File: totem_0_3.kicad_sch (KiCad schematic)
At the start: 52 parts, among them J1 MJ-4PP-9, J2 MJ-4PP-9, U1 xiao-ble, U2 xiao-ble, U3 RP2040, U4 RP2040

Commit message: Split MCU aux schemas into own sheet
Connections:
- net GND_L: now also U3.57 (GND)
- net GND_R: now also U4.57 (GND)
- net 3V3_REG_L: now reaches U3.1 (IOVDD), U3.10 (IOVDD), U3.22 (IOVDD), U3.33 (IOVDD), U3.42 (IOVDD), U3.49 (IOVDD)
- net 3V3_REG_L: now also U3.43 (ADC_AVDD), U3.44 (VREG_IN), U3.48 (USB_VDD)
- net XIN_L: now reaches U3.20 (XIN)
- net XOUT_L: now reaches U3.21 (XOUT)
- net USB_L_D-: now reaches U3.46 (USB_DM)
- net USB_L_D-: now also U4.46 (USB_DM)
- net USB_L_D+: now reaches U3.47 (USB_DP)
- net USB_L_D+: now also U4.47 (USB_DP)
- net 3V3_REG_R: now reaches U4.1 (IOVDD), U4.10 (IOVDD), U4.22 (IOVDD), U4.33 (IOVDD), U4.42 (IOVDD), U4.49 (IOVDD)
- net 3V3_REG_R: now also U4.43 (ADC_AVDD), U4.44 (VREG_IN), U4.48 (USB_VDD)
- net XIN_R: now reaches U4.20 (XIN)
- net XOUT_R: now reaches U4.21 (XOUT)
- net VREG_R: now reaches U4.23 (DVDD), U4.50 (DVDD)
- net VREG_R: now also U4.45 (VREG_VOUT)
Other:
- added sheet MCU auxiliaries (mcu_auxiliaries.kicad_sch)
- moved on the sheet: BAT+1, BAT+2, BATGND1, BATGND2, J1, J2, PSW1, PSW2, RSW1, RSW2, SWL1, SWL10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

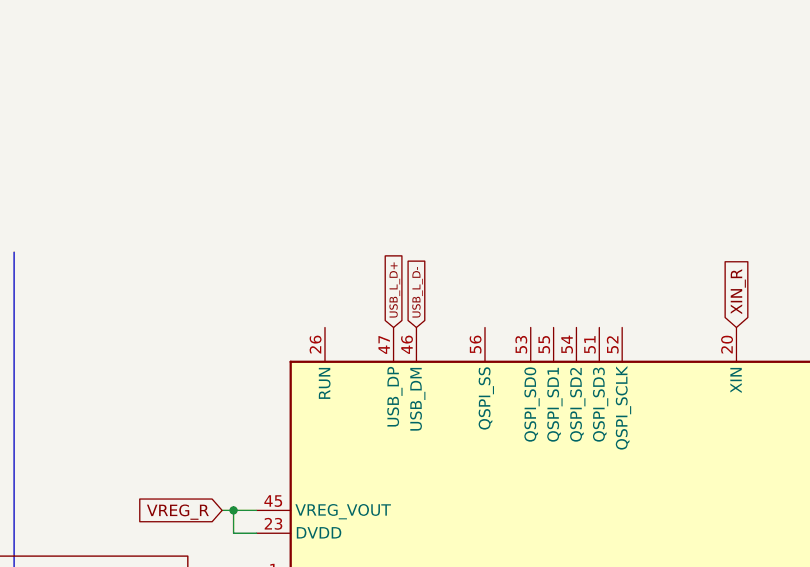
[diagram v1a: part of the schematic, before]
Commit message: fix right usb labels
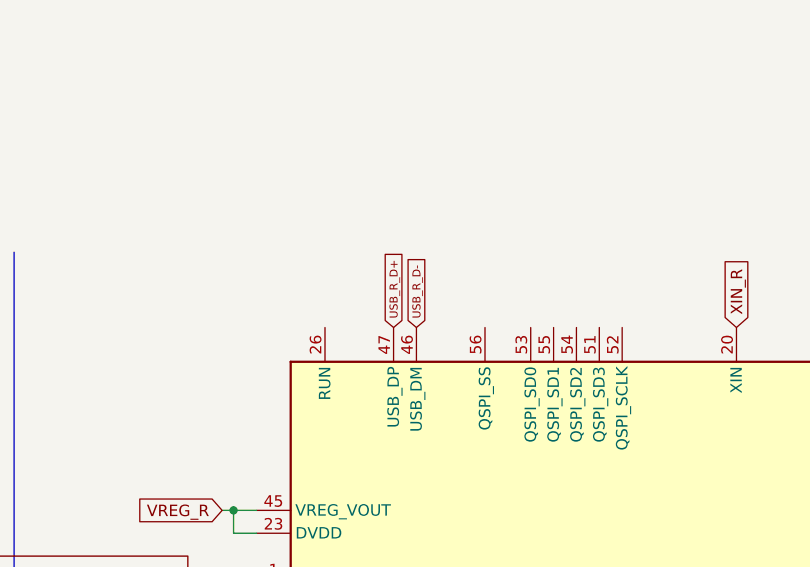
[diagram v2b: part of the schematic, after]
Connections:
- net USB_L_D+: no longer U4.47 (USB_DP)
- net USB_L_D-: no longer U4.46 (USB_DM)
- new net USB_R_D+: U4.47 (USB_DP)
- new net USB_R_D-: U4.46 (USB_DM)
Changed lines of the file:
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@@
 		)
 	)
-	(global_label "USB_L_D-"
+	(global_label "USB_R_D-"
 		(shape input)
 		(at 193.04 20.32 90)
@@
 		)
 		(property "Intersheetrefs" "${INTERSHEET_REFS}"
-			(at 193.04 11.4995 90)
+			(at 193.04 11.3302 90)
 			(effects
 				(font
@@
 		)
 	)
-	(global_label "USB_L_D+"
+	(global_label "USB_R_D+"
 		(shape input)
 		(at 190.5 20.32 90)
@@
 		)
 		(property "Intersheetrefs" "${INTERSHEET_REFS}"
-			(at 190.5 11.4995 90)
+			(at 190.5 11.3302 90)
 			(effects
 				(font

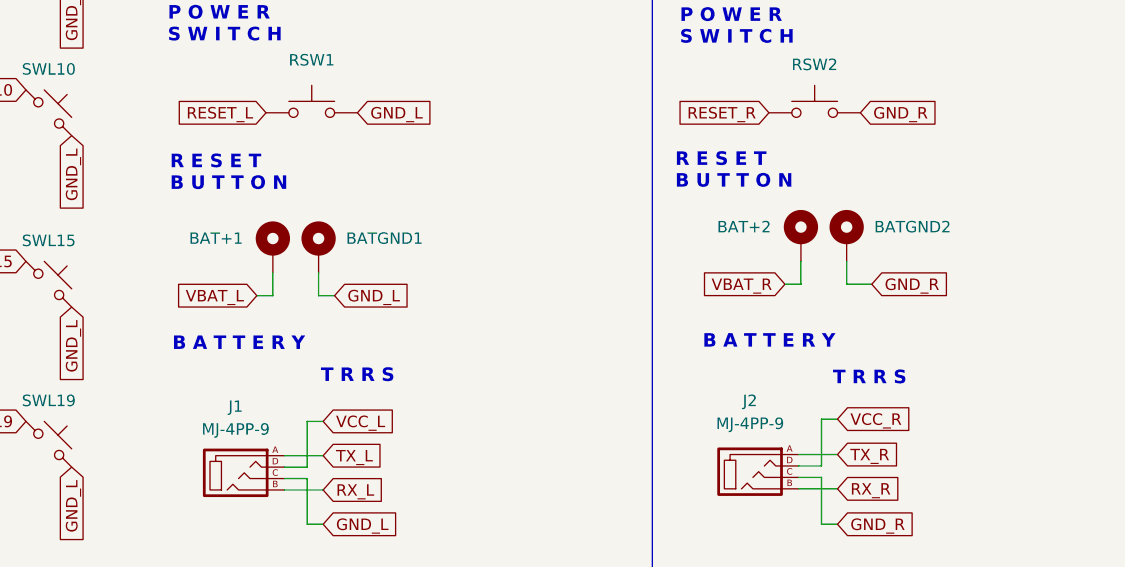
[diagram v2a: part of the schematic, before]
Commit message: Remove battery from schema
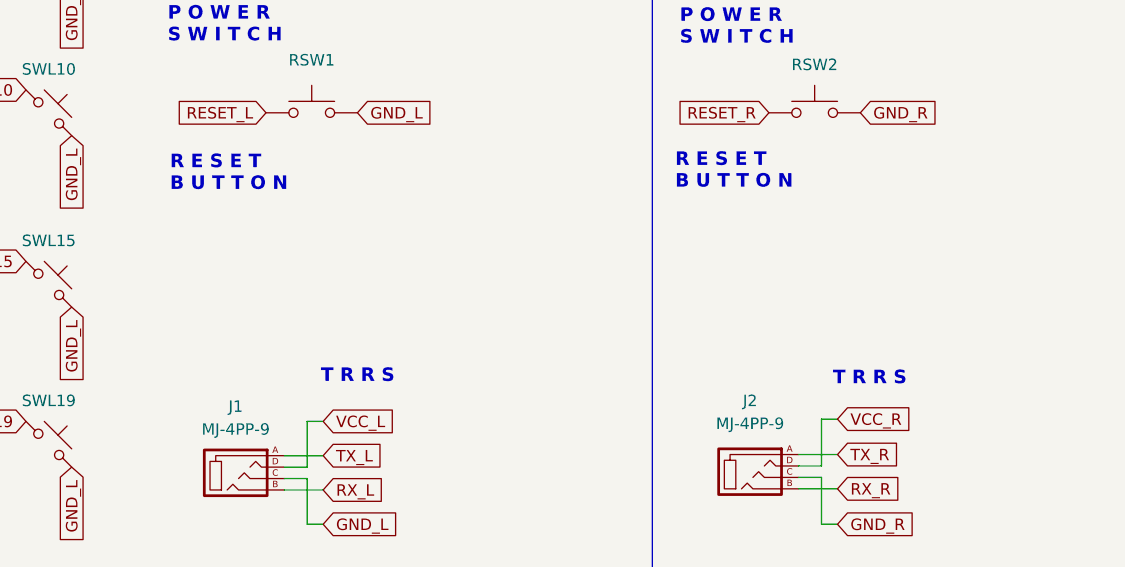
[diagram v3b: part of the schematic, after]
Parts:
- removed BAT+1, BAT+2: +, TOTEMlib:BatteryPad, symbol Mechanical:MountingHole_Pad
- removed BATGND1, BATGND2: -, TOTEMlib:BatteryPad, symbol Mechanical:MountingHole_Pad
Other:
- note removed: "B A T T E R Y"

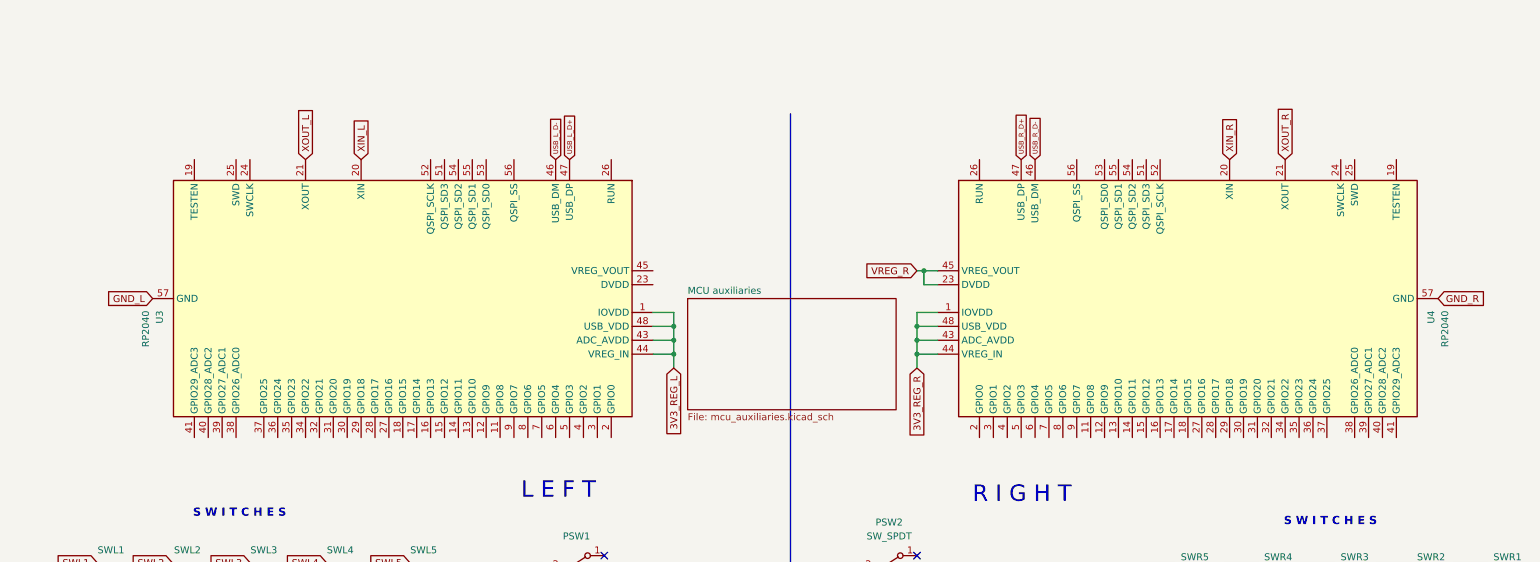
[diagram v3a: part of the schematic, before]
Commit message: Add qspi flash
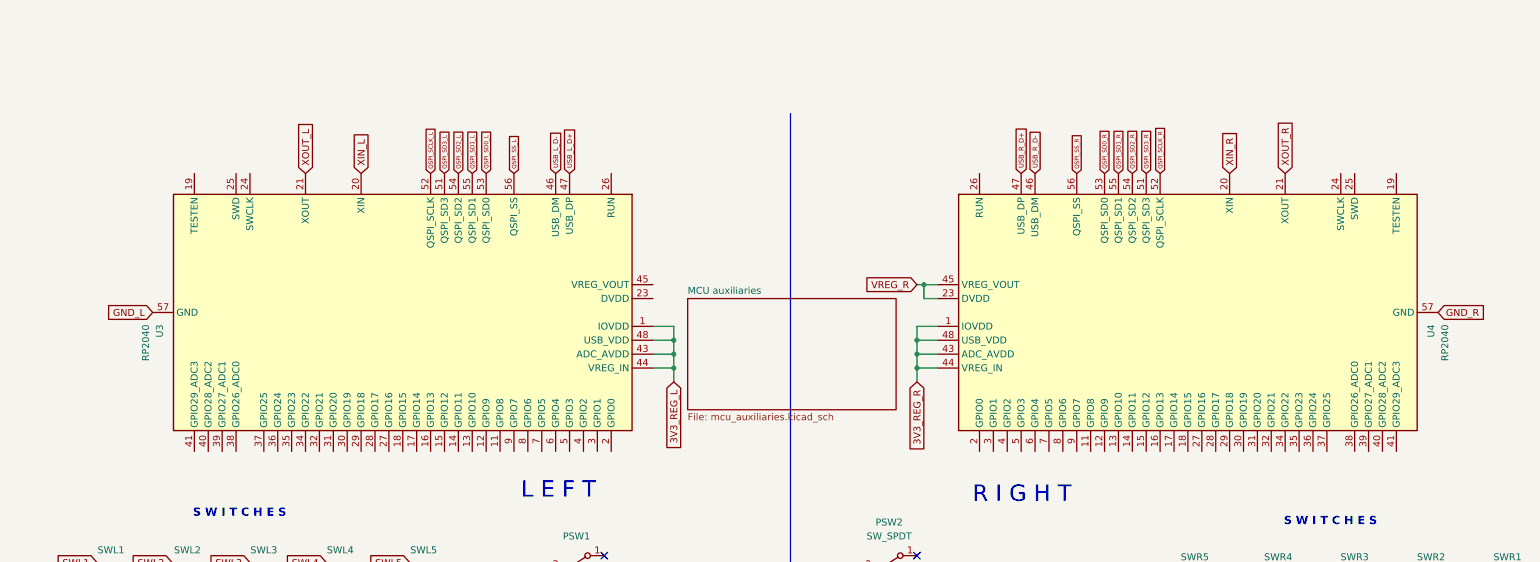
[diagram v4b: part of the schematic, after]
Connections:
- net QSPI_SD3_L: now reaches U3.51 (QSPI_SD3)
- net QSPI_SCLK_L: now reaches U3.52 (QSPI_SCLK)
- net QSPI_SD0_L: now reaches U3.53 (QSPI_SD0)
- net QSPI_SD2_L: now reaches U3.54 (QSPI_SD2)
- net QSPI_SD1_L: now reaches U3.55 (QSPI_SD1)
- net QSPI_SS_L: now reaches U3.56 (QSPI_SS)
- net QSPI_SD3_R: now reaches U4.51 (QSPI_SD3)
- net QSPI_SCLK_R: now reaches U4.52 (QSPI_SCLK)
- net QSPI_SD0_R: now reaches U4.53 (QSPI_SD0)
- net QSPI_SD2_R: now reaches U4.54 (QSPI_SD2)
- net QSPI_SD1_R: now reaches U4.55 (QSPI_SD1)
- net QSPI_SS_R: now reaches U4.56 (QSPI_SS)
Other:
- moved on the sheet: U3, U4

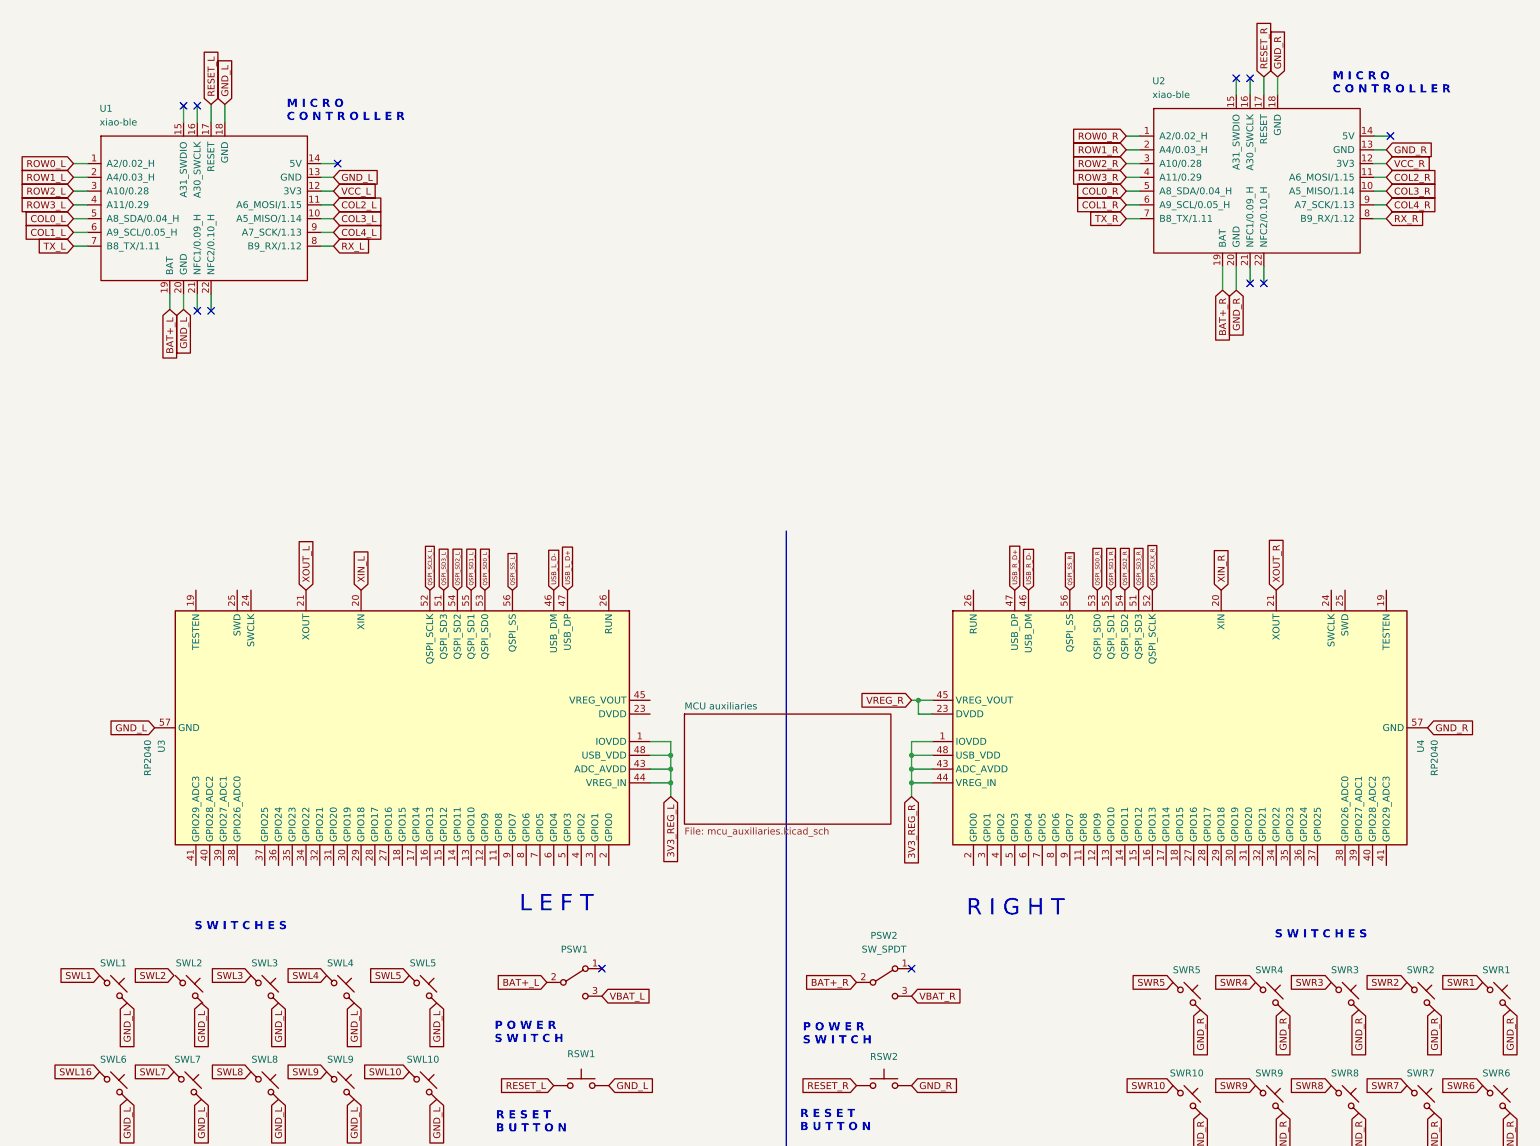
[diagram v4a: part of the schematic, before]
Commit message: Remove old mcu
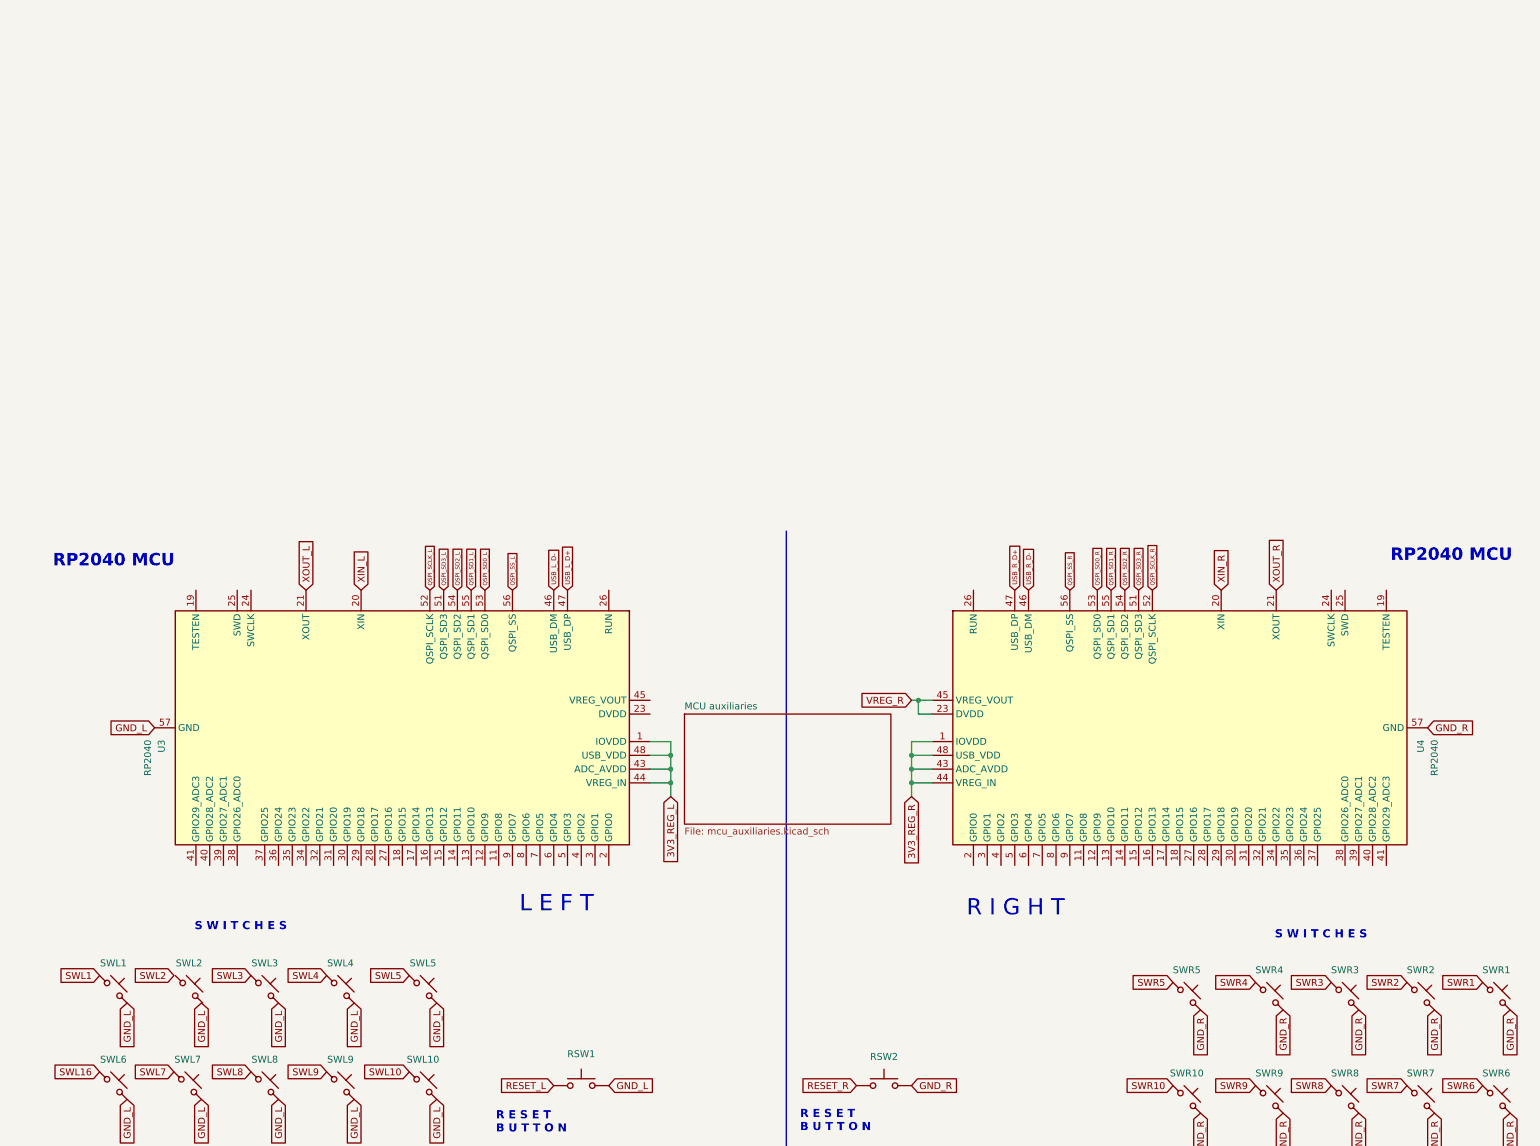
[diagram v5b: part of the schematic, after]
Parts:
- removed PSW1, PSW2: SW_SPDT, TOTEMlib:MSK12C02, symbol Switch:SW_SPDT
- removed U1, U2: xiao-ble, TOTEMlib:xiao-ble-smd-cutout, symbol mcu:xiao-ble
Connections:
- no-connect marks 12 -> 0
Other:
- note added: "RP2040 MCU"
- note removed: "M I C R O C O N T R O L L E R"
- note removed: "P O W E R S W I T C H"

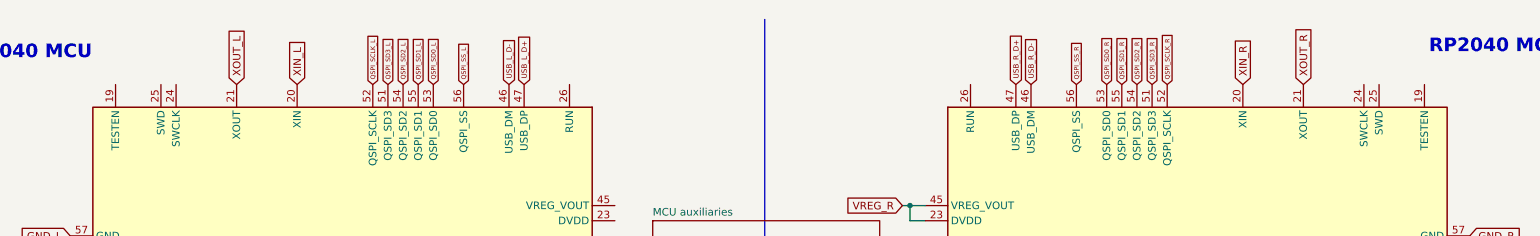
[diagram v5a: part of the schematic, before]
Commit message: Hook up reset pins
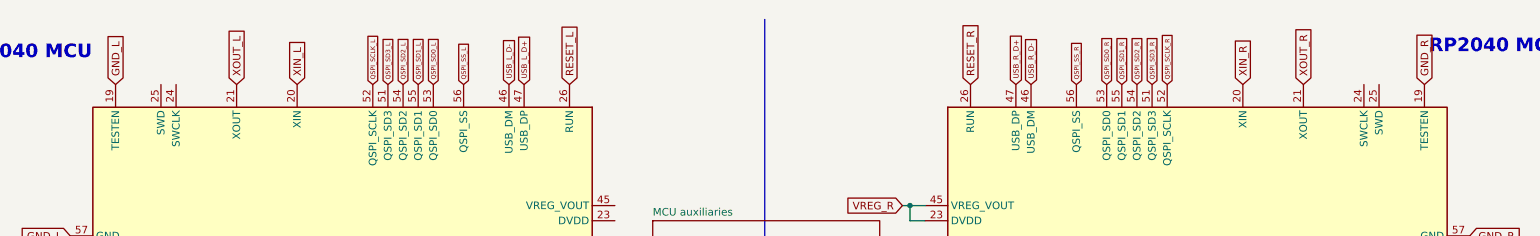
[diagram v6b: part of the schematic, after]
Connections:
- net GND_L: now also U3.19 (TESTEN)
- net GND_R: now also U4.19 (TESTEN)
- net RESET_L: now also U3.26 (RUN)
- net RESET_R: now also U4.26 (RUN)
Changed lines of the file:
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@@
+		)
+	)
+	(global_label "GND_R"
+		(shape input)
+		(at 259.08 22.86 90)
+		(fields_autoplaced yes)
+		(effects
+			(font
+				(size 1.27 1.27)
+			)
+			(justify left)
+		)
+		(property "Intersheetrefs" "${INTERSHEET_REFS}"
+			(at 259.08 13.7667 90)
+			(effects
+				(font
+					(size 1.27 1.27)
+				)
+				(justify left)
+				(hide yes)
+			)
 		)
 	)
@@
 		)
 	)
+	(global_label "RESET_R"
+		(shape input)
+		(at 182.88 22.86 90)
+		(fields_autoplaced yes)
+		(effects
+			(font
+				(size 1.27 1.27)
+			)
+			(justify left)
+		)
+		(property "Intersheetrefs" "${INTERSHEET_REFS}"
+			(at 182.88 11.8921 90)
+			(effects
+				(font
+					(size 1.27 1.27)
+				)
+				(justify left)
+				(hide yes)
+			)
+		)
+	)
 	(global_label "VREG_R"
 		(shape input)
@@
 		)
 	)
+	(global_label "GND_L"
+		(shape input)
+		(at 39.37 22.86 90)
+		(fields_autoplaced yes)
+		(effects
+			(font
+				(size 1.27 1.27)
+			)
+			(justify left)
+		)
+		(property "Intersheetrefs" "${INTERSHEET_REFS}"
+			(at 39.37 14.0086 90)
+			(effects
+				(font
+					(size 1.27 1.27)
+				)
+				(justify left)
+				(hide yes)
+			)
+		)
+	)
 	(global_label "GND_R"
 		(shape input)
@@
 				(hide yes)
 			)
+		)
+	)
+	(global_label "RESET_L"
+		(shape input)
+		(at 115.57 22.86 90)
+		(fields_autoplaced yes)
+		(effects
+			(font
+				(size 1.27 1.27)
+			)
+			(justify left)
+		)
+		(property "Intersheetrefs" "${INTERSHEET_REFS}"
+			(at 115.57 12.134 90)
+			(effects
+				(font
+					(size 1.27 1.27)
+				)
+				(justify left)
+				(hide yes)
+			)
